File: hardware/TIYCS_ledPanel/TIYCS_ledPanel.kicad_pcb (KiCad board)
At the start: 2 copper layers, 100 x 100 mm, 8 parts

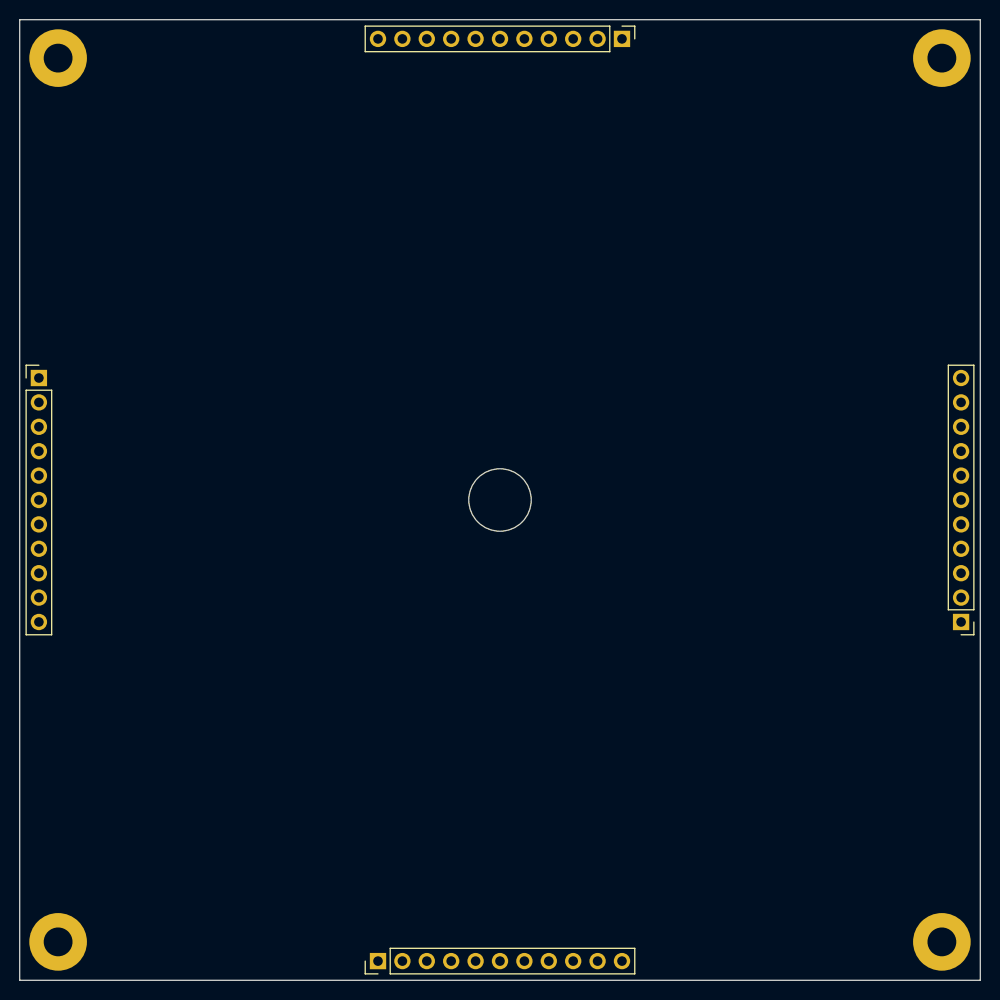
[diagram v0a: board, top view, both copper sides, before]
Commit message: Placement of LEDs
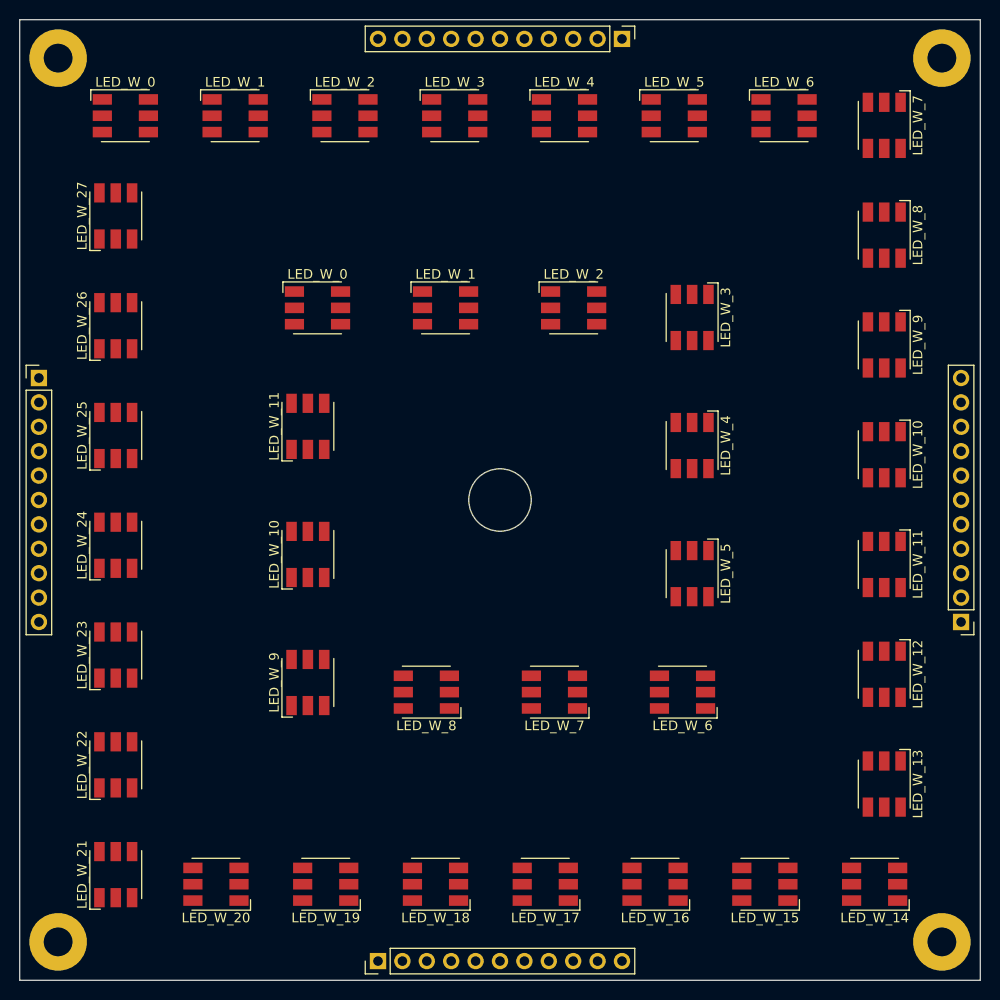
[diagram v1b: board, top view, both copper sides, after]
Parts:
- added LED_W_0: LED_RGB_5050-6, LED_RGB_5050-6, F.Cu at (-19.0, -20.0)
- added LED_W_0: LED_RGB_5050-6, LED_RGB_5050-6, F.Cu at (-39.0, -40.0)
- added LED_W_1: LED_RGB_5050-6, LED_RGB_5050-6, F.Cu at (-27.6, -40.0)
- added LED_W_1: LED_RGB_5050-6, LED_RGB_5050-6, F.Cu at (-5.67, -20.0)
- added LED_W_10: LED_RGB_5050-6, LED_RGB_5050-6, F.Cu at (40.0, -4.71)
- added LED_W_10: LED_RGB_5050-6, LED_RGB_5050-6, F.Cu at (-20.0, 5.67)
- added LED_W_11: LED_RGB_5050-6, LED_RGB_5050-6, F.Cu at (40.0, 6.71)
- added LED_W_11: LED_RGB_5050-6, LED_RGB_5050-6, F.Cu at (-20.0, -7.67)
- added LED_W_12: LED_RGB_5050-6, LED_RGB_5050-6, F.Cu at (40.0, 18.1)
- added LED_W_13: LED_RGB_5050-6, LED_RGB_5050-6, F.Cu at (40.0, 29.6)
- added LED_W_14: LED_RGB_5050-6, LED_RGB_5050-6, F.Cu at (39.0, 40.0)
- added LED_W_15: LED_RGB_5050-6, LED_RGB_5050-6, F.Cu at (27.6, 40.0)
- added LED_W_16: LED_RGB_5050-6, LED_RGB_5050-6, F.Cu at (16.1, 40.0)
- added LED_W_17: LED_RGB_5050-6, LED_RGB_5050-6, F.Cu at (4.71, 40.0)
- added LED_W_18: LED_RGB_5050-6, LED_RGB_5050-6, F.Cu at (-6.71, 40.0)
- added LED_W_19: LED_RGB_5050-6, LED_RGB_5050-6, F.Cu at (-18.1, 40.0)
- added LED_W_2: LED_RGB_5050-6, LED_RGB_5050-6, F.Cu at (7.67, -20.0)
- added LED_W_2: LED_RGB_5050-6, LED_RGB_5050-6, F.Cu at (-16.1, -40.0)
- added LED_W_20: LED_RGB_5050-6, LED_RGB_5050-6, F.Cu at (-29.6, 40.0)
- added LED_W_21: LED_RGB_5050-6, LED_RGB_5050-6, F.Cu at (-40.0, 39.0)
- added LED_W_22: LED_RGB_5050-6, LED_RGB_5050-6, F.Cu at (-40.0, 27.6)
- added LED_W_23: LED_RGB_5050-6, LED_RGB_5050-6, F.Cu at (-40.0, 16.1)
- added LED_W_24: LED_RGB_5050-6, LED_RGB_5050-6, F.Cu at (-40.0, 4.71)
- added LED_W_25: LED_RGB_5050-6, LED_RGB_5050-6, F.Cu at (-40.0, -6.71)
- added LED_W_26: LED_RGB_5050-6, LED_RGB_5050-6, F.Cu at (-40.0, -18.1)
- added LED_W_27: LED_RGB_5050-6, LED_RGB_5050-6, F.Cu at (-40.0, -29.6)
- added LED_W_3: LED_RGB_5050-6, LED_RGB_5050-6, F.Cu at (-4.71, -40.0)
- added LED_W_3: LED_RGB_5050-6, LED_RGB_5050-6, F.Cu at (20.0, -19.0)
- added LED_W_4: LED_RGB_5050-6, LED_RGB_5050-6, F.Cu at (20.0, -5.67)
- added LED_W_4: LED_RGB_5050-6, LED_RGB_5050-6, F.Cu at (6.71, -40.0)
- added LED_W_5: LED_RGB_5050-6, LED_RGB_5050-6, F.Cu at (20.0, 7.67)
- added LED_W_5: LED_RGB_5050-6, LED_RGB_5050-6, F.Cu at (18.1, -40.0)
- added LED_W_6: LED_RGB_5050-6, LED_RGB_5050-6, F.Cu at (29.6, -40.0)
- added LED_W_6: LED_RGB_5050-6, LED_RGB_5050-6, F.Cu at (19.0, 20.0)
- added LED_W_7: LED_RGB_5050-6, LED_RGB_5050-6, F.Cu at (40.0, -39.0)
- added LED_W_7: LED_RGB_5050-6, LED_RGB_5050-6, F.Cu at (5.67, 20.0)
- added LED_W_8: LED_RGB_5050-6, LED_RGB_5050-6, F.Cu at (-7.67, 20.0)
- added LED_W_8: LED_RGB_5050-6, LED_RGB_5050-6, F.Cu at (40.0, -27.6)
- added LED_W_9: LED_RGB_5050-6, LED_RGB_5050-6, F.Cu at (40.0, -16.1)
- added LED_W_9: LED_RGB_5050-6, LED_RGB_5050-6, F.Cu at (-20.0, 19.0)
